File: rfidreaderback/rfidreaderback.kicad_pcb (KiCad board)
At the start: 2 copper layers, 42 x 40 mm, 12 parts, among them P1 READER, P2 PI, U1 LD1117S50TR, U2 ST232BDR

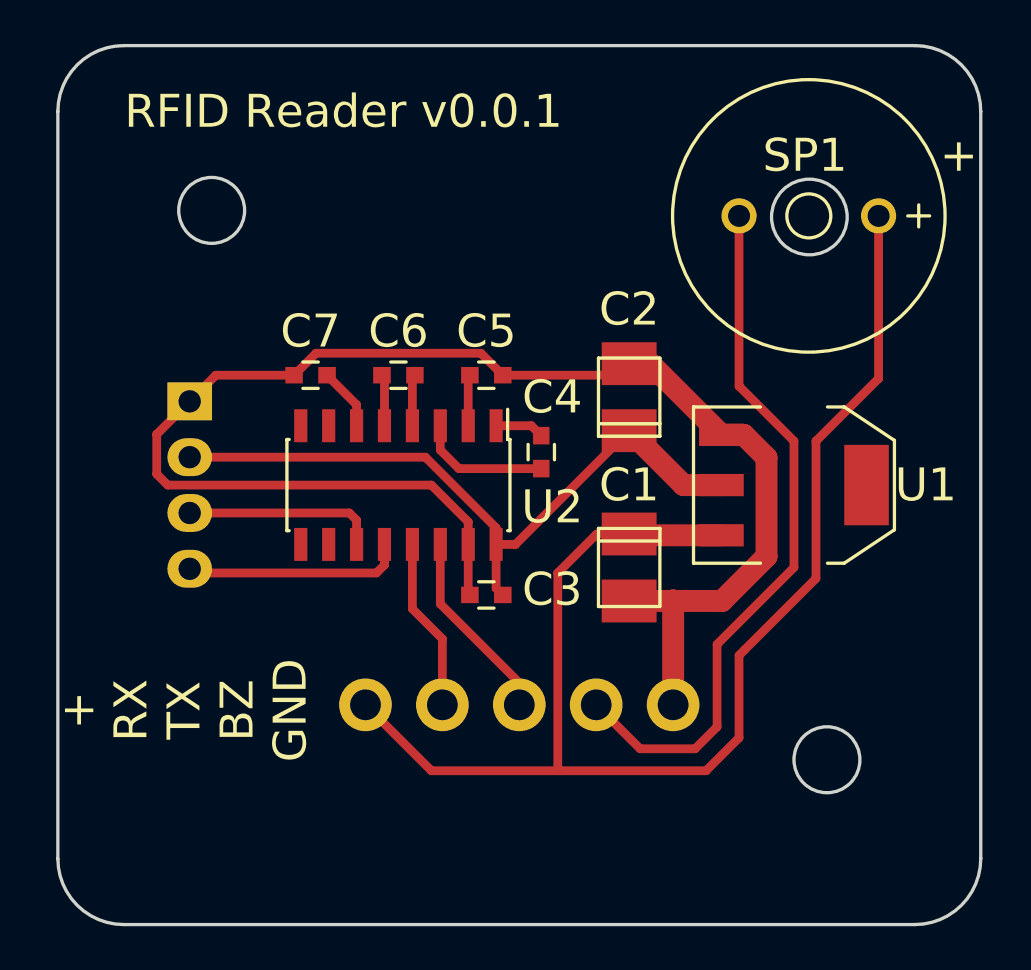
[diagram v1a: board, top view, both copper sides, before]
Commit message: Probably best if the level converters are connected to the correct level
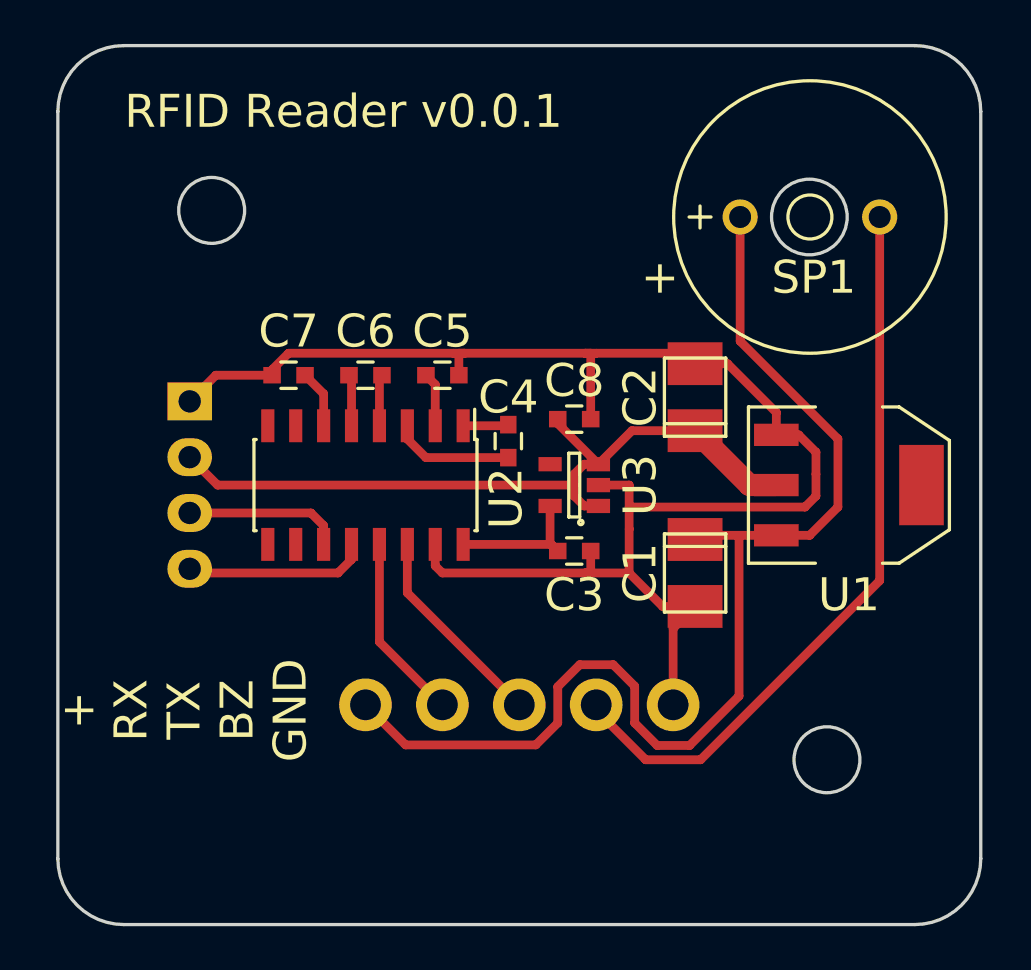
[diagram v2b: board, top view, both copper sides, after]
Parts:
- added C8: 1µ, Capacitors_SMD:C_0603, F.Cu at (154.5, 113.0)
- added U3: MIC5317-3.3YM5, TO_SOT_Packages_SMD:SOT-23-5, F.Cu at (154.5, 116.0)
- U2: value ST232BDR -> ST3232BDR
- moved SP1 6.40 mm to (168.4, 103.8), turned to 180 degrees
- moved C3 4.47 mm to (154.5, 119.0), turned to 180 degrees
- moved C1 3.01 mm to (160.0, 120.0)
- moved C2 3.00 mm to (160.0, 112.0)
- moved U1 2.50 mm to (167.0, 116.0)
- moved C5 2.00 mm to (148.5, 111.0)
- moved C4 1.58 mm to (151.5, 114.0)
- moved C6 1.50 mm to (145.0, 111.0)
- moved U2 1.50 mm to (145.0, 116.0)
- moved C7 1.00 mm to (141.5, 111.0)
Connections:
- C3 pad 2: +5V -> +3V3
- U2 pad 16: +5V -> +3V3
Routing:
- net +12V: track 62.5 -> 53.4 mm
- net +3V3: track 0.00 -> 6.62 mm
- net GND: track 70.4 -> 74.1 mm
- net +5V: track 32.9 -> 34.9 mm
- net /TXD: track 8.83 -> 7.19 mm
- net /buzzer: track 32.5 -> 34.0 mm
- net /RXD: track 10.0 -> 8.65 mm
- net /EIA-TX: track 8.79 -> 9.41 mm
- net /EIA-RX: track 7.87 -> 8.49 mm
- net Net-(C4-Pad2): track 6.05 -> 5.55 mm

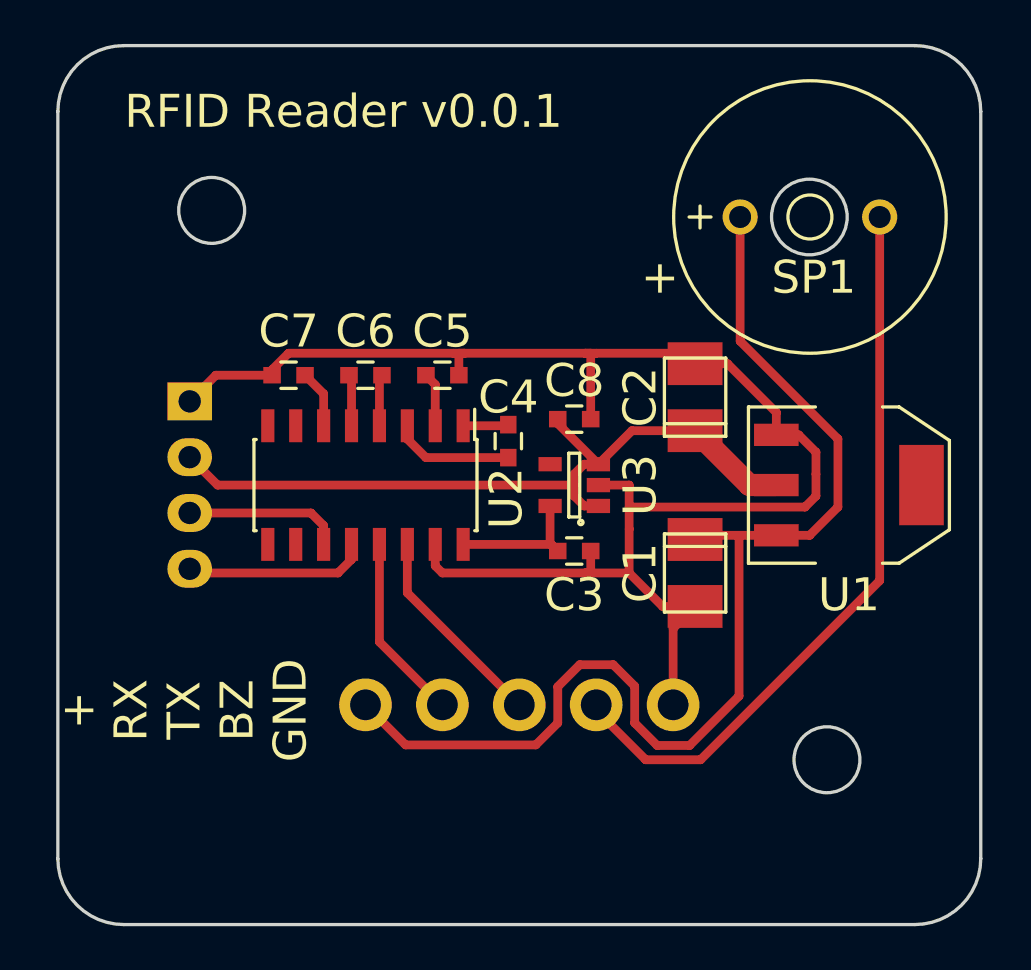
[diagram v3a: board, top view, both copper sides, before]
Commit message: switch unnecisarry milling to drill
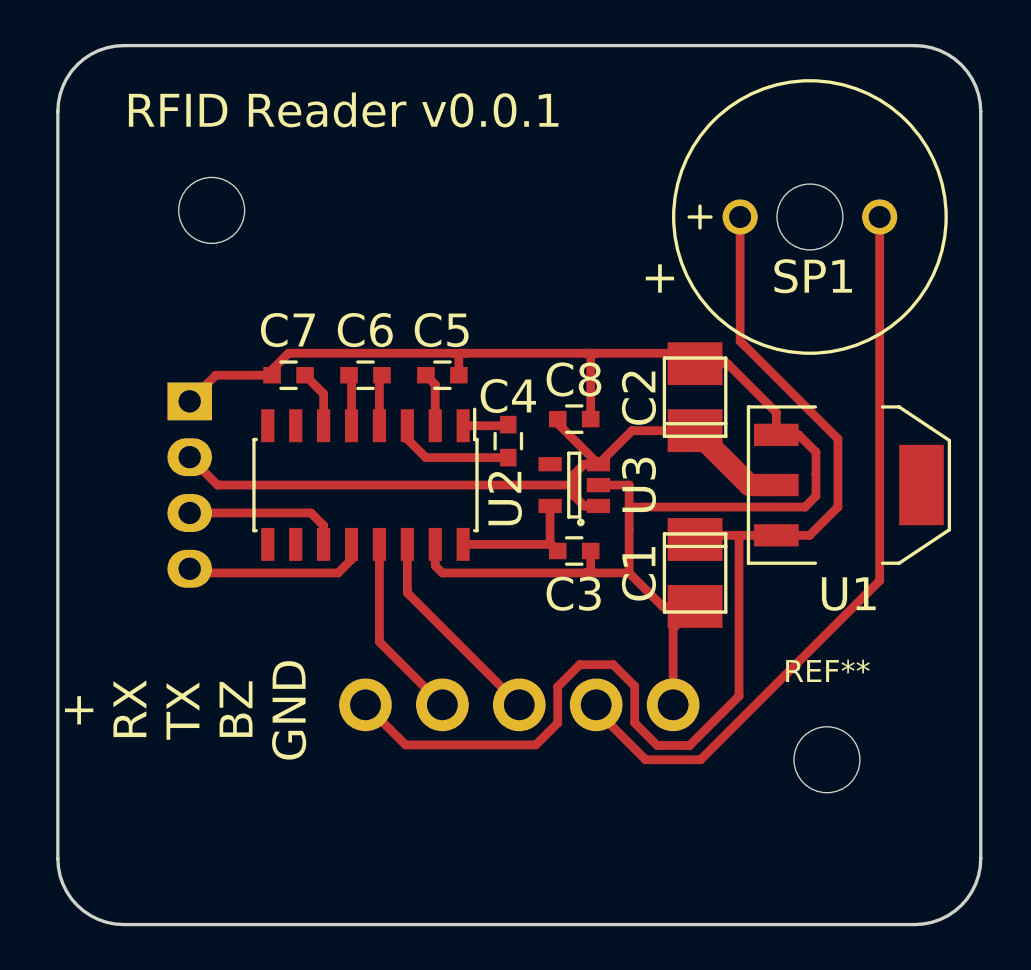
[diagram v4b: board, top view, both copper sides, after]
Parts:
- added REF**: MountingHole_3mm, Mounting_Holes:MountingHole_3mm, F.Cu at (166.0, 128.5)
- added REF**: MountingHole_3mm, Mounting_Holes:MountingHole_3mm, F.Cu at (138.0, 103.5)
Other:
- outline, holes or cut-outs redrawn
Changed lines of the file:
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@@
     (links 31)
     (no_connects 0)
-    (area 130.625 95.924999 174.082143 136.075001)
+    (area 130.924999 95.924999 173.075001 136.075001)
     (thickness 1.6)
-    (drawings 15)
+    (drawings 10)
     (tracks 112)
     (zones 0)
-    (modules 14)
+    (modules 16)
     (nets 16)
   )
@@
     (mod_text_size 1.5 1.5)
     (mod_text_width 0.25)
-    (pad_size 3.6576 2.032)
-    (pad_drill 0)
+    (pad_size 3 3)
+    (pad_drill 3)
     (pad_to_mask_clearance 0)
     (aux_axis_origin 131 136)
@@
     (uvia_drill 0.1)
   )
+  (module Buzzers_Beepers:MagneticBuzzer_ProSignal_ABT-410-RC (layer F.Cu)
+    (at 168.4 103.8 180)
+    (descr "Buzzer, Elektromagnetic Beeper, Summer, 1,5V-DC,")
+    (tags "Pro Signal, ABT-410-RC,")
+    (fp_text reference SP1 (at 3 -2.75 180) (layer F.SilkS)
+      (effects (font (size 1.5 1.5) (thickness 0.25)))
+    )
+    (fp_text value MCABI-020-RC (at 3.5 -2.75 180) (layer F.Fab)
+      (effects (font (size 1.5 1.5) (thickness 0.25)))
+    )
+    (fp_line (start 8.17626 -0.50038) (end 8.17626 0.50038) (layer F.SilkS) (width 0.15))
+    (fp_line (start 7.67588 0) (end 8.6741 0) (layer F.SilkS) (width 0.15))
+    (fp_text user + (at 10 -2.75 180) (layer F.SilkS)
+      (effects (font (size 1.5 1.5) (thickness 0.25)))
+    )
+    (fp_circle (center 3.175 0) (end 9.37514 0) (layer F.SilkS) (width 0.15))
+    (pad 1 thru_hole circle (at 0 0 180) (size 1.6002 1.6002) (drill 1.00076) (layers *.Cu *.Mask F.SilkS)
+      (net 13 /buzzer))
+    (pad 2 thru_hole circle (at 6.35 0 180) (size 1.6002 1.6002) (drill 1.00076) (layers *.Cu *.Mask F.SilkS)
+      (net 3 +12V))
+    (pad "" np_thru_hole circle (at 3.175 0 180) (size 3 3) (drill 3) (layers *.Cu *.Mask))
+    (model Buzzers_Beepers.3dshapes/MagneticBuzzer_ProSignal_ABT-410-RC.wrl
+      (at (xyz 0 0 0))
+      (scale (xyz 1 1 1))
+      (rotate (xyz 0 0 0))
+    )
+  )
+  (module Mounting_Holes:MountingHole_3mm (layer F.Cu)
+    (at 166 128.5)
+    (descr "Mounting hole, Befestigungsbohrung, 3mm, No Annular, Kein Restring,")
+    (tags "Mounting hole, Befestigungsbohrung, 3mm, No Annular, Kein Restring,")
+    (fp_text reference REF** (at 0 -4.0005) (layer F.SilkS)
+      (effects (font (size 1 1) (thickness 0.15)))
+    )
+    (fp_text value MountingHole_3mm (at 1.00076 5.00126) (layer F.Fab)
+      (effects (font (size 1 1) (thickness 0.15)))
+    )
+    (fp_circle (center 0 0) (end 3 0) (layer Cmts.User) (width 0.381))
+    (pad "" np_thru_hole circle (at 0 0) (size 3 3) (drill 3) (layers *.Cu *.Mask))
+  )
+  (module Mounting_Holes:MountingHole_3mm (layer F.Cu)
+    (at 138 103.5)
+    (descr "Mounting hole, Befestigungsbohrung, 3mm, No Annular, Kein Restring,")
+    (tags "Mounting hole, Befestigungsbohrung, 3mm, No Annular, Kein Restring,")
+    (fp_text reference REF** (at 0 -4.0005) (layer F.SilkS) hide
+      (effects (font (size 1 1) (thickness 0.15)))
+    )
+    (fp_text value MountingHole_3mm (at 1.00076 5.00126) (layer F.Fab)
+      (effects (font (size 1 1) (thickness 0.15)))
+    )
+    (fp_circle (center 0 0) (end 3 0) (layer Cmts.User) (width 0.381))
+    (pad "" np_thru_hole circle (at 0 0) (size 3 3) (drill 3) (layers *.Cu *.Mask))
+  )
   (module TO_SOT_Packages_SMD:SOT-23-5 (layer F.Cu)
     (at 154.5 116 180)
@@
       (net 9 "Net-(C7-Pad2)"))
     (model Capacitors_SMD.3dshapes/C_0603.wrl
-      (at (xyz 0 0 0))
-      (scale (xyz 1 1 1))
-      (rotate (xyz 0 0 0))
-    )
-  )
-  (module Buzzers_Beepers:MagneticBuzzer_ProSignal_ABT-410-RC (layer F.Cu)
-    (at 168.4 103.8 180)
-    (descr "Buzzer, Elektromagnetic Beeper, Summer, 1,5V-DC,")
-    (tags "Pro Signal, ABT-410-RC,")
-    (fp_text reference SP1 (at 3 -2.75 180) (layer F.SilkS)
-      (effects (font (size 1.5 1.5) (thickness 0.25)))
-    )
-    (fp_text value MCABI-020-RC (at 3.5 -2.75 180) (layer F.Fab)
-      (effects (font (size 1.5 1.5) (thickness 0.25)))
-    )
-    (fp_line (start 8.17626 -0.50038) (end 8.17626 0.50038) (layer F.SilkS) (width 0.15))
-    (fp_line (start 7.67588 0) (end 8.6741 0) (layer F.SilkS) (width 0.15))
-    (fp_circle (center 3.175 0) (end 4.17576 0) (layer F.SilkS) (width 0.15))
-    (fp_text user + (at 10 -2.75 180) (layer F.SilkS)
-      (effects (font (size 1.5 1.5) (thickness 0.25)))
-    )
-    (fp_circle (center 3.175 0) (end 9.37514 0) (layer F.SilkS) (width 0.15))
-    (pad 1 thru_hole circle (at 0 0 180) (size 1.6002 1.6002) (drill 1.00076) (layers *.Cu *.Mask F.SilkS)
-      (net 13 /buzzer))
-    (pad 2 thru_hole circle (at 6.35 0 180) (size 1.6002 1.6002) (drill 1.00076) (layers *.Cu *.Mask F.SilkS)
-      (net 3 +12V))
-    (model Buzzers_Beepers.3dshapes/MagneticBuzzer_ProSignal_ABT-410-RC.wrl
       (at (xyz 0 0 0))
       (scale (xyz 1 1 1))
@@
     (effects (font (size 1.5 1.5) (thickness 0.25)))
   )
-  (gr_circle (center 165.2 103.8) (end 166.6 104.8) (layer Edge.Cuts) (width 0.15))
-  (gr_circle (center 138 103.5) (end 141 103.5) (layer Dwgs.User) (width 0.2))
-  (gr_circle (center 166 128.5) (end 169 128.5) (layer Dwgs.User) (width 0.2))
-  (gr_circle (center 138 103.5) (end 139.5 103.5) (layer Edge.Cuts) (width 0.15))
-  (gr_circle (center 166 128.5) (end 166 130) (layer Edge.Cuts) (width 0.15))
   (gr_line (start 134 96) (end 170 96) (angle 90) (layer Edge.Cuts) (width 0.15))
   (gr_arc (start 134 99) (end 131 99) (angle 90) (layer Edge.Cuts) (width 0.15))

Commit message: gnd unused inputs
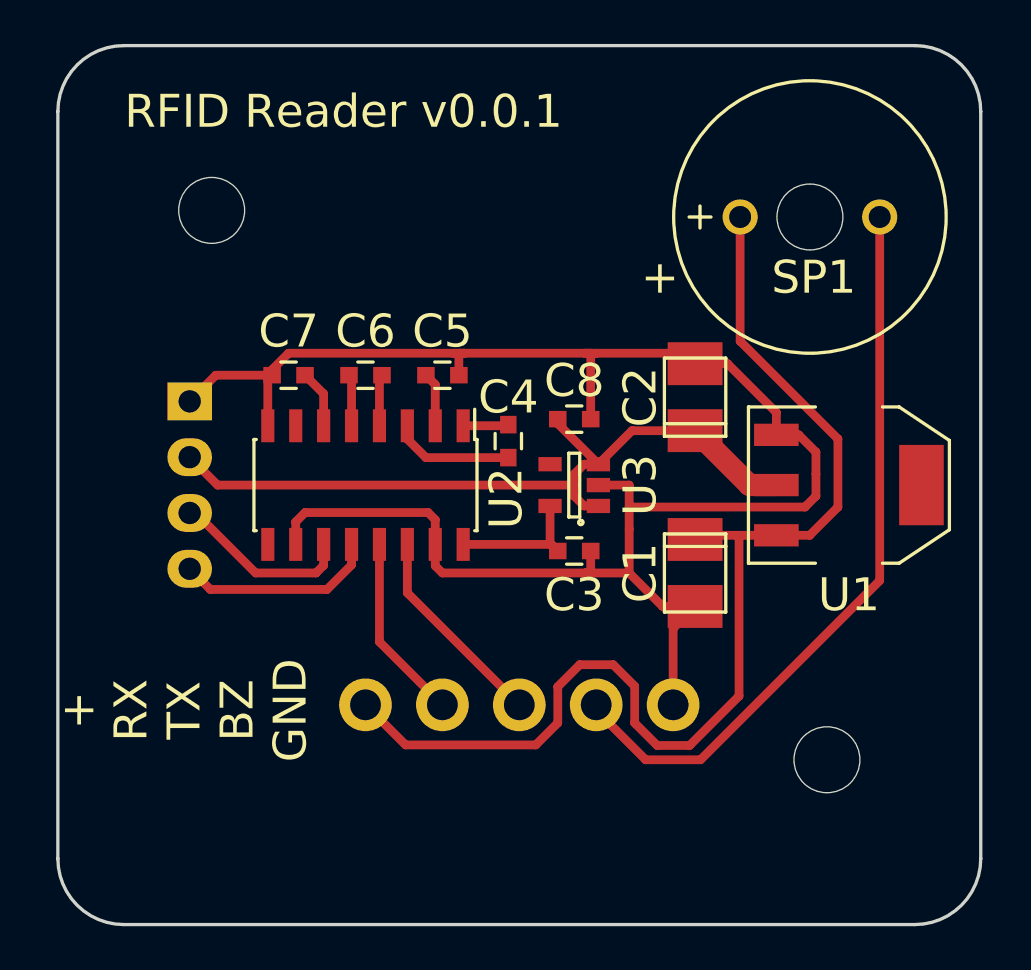
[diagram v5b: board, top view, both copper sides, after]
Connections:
- U2 pad 10: (no net) -> GND
- U2 pad 8: (no net) -> GND
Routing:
- net GND: track 74.1 -> 85.3 mm
- net /TXD: track 7.19 -> 8.32 mm
- net /RXD: track 8.65 -> 9.69 mm
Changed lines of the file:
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@@
 (kicad_pcb (version 4) (host pcbnew 4.0.2+dfsg1-stable)
   (general
-    (links 31)
+    (links 33)
     (no_connects 0)
-    (area 130.924999 95.924999 173.075001 136.075001)
+    (area 130.625 95.924999 174.490046 136.075001)
     (thickness 1.6)
     (drawings 10)
-    (tracks 112)
+    (tracks 122)
     (zones 0)
     (modules 16)
@@
     (title "RFID Reader Back")
     (date 2016-09-30)
-    (rev 0.0.1)
+    (rev 0.0.2)
     (company "©2016 Wirehive ltd, CC BY-SA ")
   )
@@
     (descr "Mounting hole, Befestigungsbohrung, 3mm, No Annular, Kein Restring,")
     (tags "Mounting hole, Befestigungsbohrung, 3mm, No Annular, Kein Restring,")
-    (fp_text reference REF** (at 0 -4.0005) (layer F.SilkS)
+    (fp_text reference REF** (at 0 -4.0005) (layer F.SilkS) hide
       (effects (font (size 1 1) (thickness 0.15)))
     )
@@
       (net 9 "Net-(C7-Pad2)"))
     (pad 7 smd rect (at -2.7 3.175 270) (size 1.5 0.6) (layers F.Cu F.Paste F.Mask))
-    (pad 8 smd rect (at -2.7 4.445 270) (size 1.5 0.6) (layers F.Cu F.Paste F.Mask))
+    (pad 8 smd rect (at -2.7 4.445 270) (size 1.5 0.6) (layers F.Cu F.Paste F.Mask)
+      (net 2 GND))
     (pad 9 smd rect (at 2.7 4.445 270) (size 1.5 0.6) (layers F.Cu F.Paste F.Mask))
-    (pad 10 smd rect (at 2.7 3.175 270) (size 1.5 0.6) (layers F.Cu F.Paste F.Mask))
+    (pad 10 smd rect (at 2.7 3.175 270) (size 1.5 0.6) (layers F.Cu F.Paste F.Mask)
+      (net 2 GND))
     (pad 11 smd rect (at 2.7 1.905 270) (size 1.5 0.6) (layers F.Cu F.Paste F.Mask)
       (net 10 /TXD))
@@
   (segment (start 163.698 116) (end 162.476 116) (width 1) (layer F.Cu) (net 1))
   (segment (start 162.476 116) (end 160 113.524) (width 1) (layer F.Cu) (net 1))
+  (segment (start 148.175 118.7) (end 148.175 117.575) (width 0.4) (layer F.Cu) (net 2))
+  (segment (start 141.825 117.675) (end 141.825 118.7) (width 0.4) (layer F.Cu) (net 2))
+  (segment (start 142.25 117.25) (end 141.825 117.675) (width 0.4) (layer F.Cu) (net 2))
+  (segment (start 147.85 117.25) (end 142.25 117.25) (width 0.4) (layer F.Cu) (net 2))
+  (segment (start 148.175 117.575) (end 147.85 117.25) (width 0.4) (layer F.Cu) (net 2))
+  (segment (start 140.555 113.3) (end 140.555 111.195) (width 0.4) (layer F.Cu) (net 2))
+  (segment (start 140.555 111.195) (end 140.75 111) (width 0.4) (layer F.Cu) (net 2))
   (segment (start 163.698 113.714) (end 164.714 113.714) (width 0.4) (layer F.Cu) (net 2))
   (segment (start 164.714 113.714) (end 165.5 114.5) (width 0.4) (layer F.Cu) (net 2))
@@
   (segment (start 143.095 113.3) (end 143.095 111.845) (width 0.4) (layer F.Cu) (net 9))
   (segment (start 143.095 111.845) (end 142.25 111) (width 0.4) (layer F.Cu) (net 9))
-  (segment (start 143.095 118.7) (end 143.095 117.845) (width 0.4) (layer F.Cu) (net 10))
-  (segment (start 142.52 117.27) (end 137 117.27) (width 0.4) (layer F.Cu) (net 10))
-  (segment (start 143.095 117.845) (end 142.52 117.27) (width 0.4) (layer F.Cu) (net 10))
-  (segment (start 144.365 118.7) (end 144.365 119.385) (width 0.4) (layer F.Cu) (net 11))
-  (segment (start 144.365 119.385) (end 143.75 120) (width 0.4) (layer F.Cu) (net 11))
-  (segment (start 143.75 120) (end 137.19 120) (width 0.4) (layer F.Cu) (net 11))
+  (segment (start 143.095 118.7) (end 143.095 119.655) (width 0.4) (layer F.Cu) (net 10))
+  (segment (start 140 120) (end 137.27 117.27) (width 0.4) (layer F.Cu) (net 10))
+  (segment (start 142.75 120) (end 140 120) (width 0.4) (layer F.Cu) (net 10))
+  (segment (start 143.095 119.655) (end 142.75 120) (width 0.4) (layer F.Cu) (net 10))
+  (segment (start 137.27 117.27) (end 137 117.27) (width 0.4) (layer F.Cu) (net 10))
+  (segment (start 144.365 118.7) (end 144.365 119.635) (width 0.4) (layer F.Cu) (net 11))
+  (segment (start 137.94 120.75) (end 137 119.81) (width 0.4) (layer F.Cu) (net 11))
+  (segment (start 143.25 120.75) (end 137.94 120.75) (width 0.4) (layer F.Cu) (net 11))
+  (segment (start 144.365 119.635) (end 143.25 120.75) (width 0.4) (layer F.Cu) (net 11))
   (segment (start 137.19 120) (end 137 119.81) (width 0.4) (layer F.Cu) (net 11))
   (segment (start 137.19 120) (end 137 119.81) (width 0.4) (layer F.Cu) (net 11))

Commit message: pre-production tweeks
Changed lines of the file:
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@@
   (gr_line (start 134 136) (end 170 136) (angle 90) (layer Edge.Cuts) (width 0.15))
   (gr_arc (start 134 133) (end 134 136) (angle 90) (layer Edge.Cuts) (width 0.15))
+  (segment (start 163.698 116) (end 162.476 116) (width 0.4) (layer F.Cu) (net 1))
+  (segment (start 162.476 116) (end 160 113.524) (width 0.4) (layer F.Cu) (net 1))
   (segment (start 153.75 113) (end 153.75 113.2) (width 0.4) (layer F.Cu) (net 1))
   (segment (start 153.75 113.2) (end 155.6 115.05) (width 0.4) (layer F.Cu) (net 1))
@@
   (segment (start 154.5 116) (end 154.5 116.5) (width 0.4) (layer F.Cu) (net 1))
   (segment (start 154.95 115.05) (end 154.5 115.5) (width 0.4) (layer F.Cu) (net 1))
-  (segment (start 163.698 116) (end 162.476 116) (width 1) (layer F.Cu) (net 1))
-  (segment (start 162.476 116) (end 160 113.524) (width 1) (layer F.Cu) (net 1))
   (segment (start 148.175 118.7) (end 148.175 117.575) (width 0.4) (layer F.Cu) (net 2))
   (segment (start 141.825 117.675) (end 141.825 118.7) (width 0.4) (layer F.Cu) (net 2))
